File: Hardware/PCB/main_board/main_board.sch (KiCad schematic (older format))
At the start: 0 parts

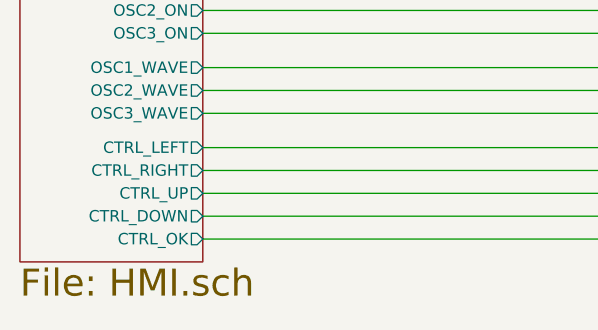
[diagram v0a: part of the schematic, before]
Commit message: Use headphone amp IC instead of discrete amp
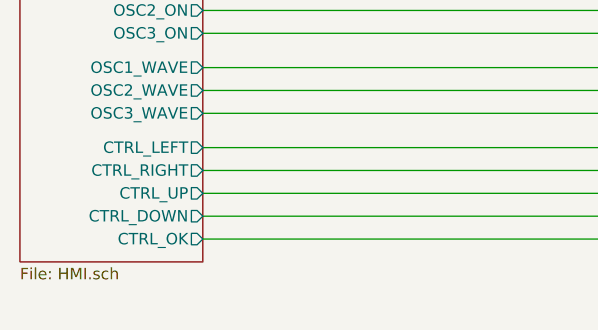
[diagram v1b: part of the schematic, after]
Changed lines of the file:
@@
 U 5E525BAF
 F0 "HMI" 118
-F1 "HMI.sch" 118
+F1 "HMI.sch" 50
 F2 "I2C_display_SDA" B R 2000 4300 50
 F3 "I2C_display_SCL" I R 2000 4400 50
